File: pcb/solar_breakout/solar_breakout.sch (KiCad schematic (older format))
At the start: 29 parts

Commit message: Initial symbol fields
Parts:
- C?: footprint (none) -> agg:0402; Farnell (none) -> 2688503
- C?: footprint (none) -> agg:0402; Farnell (none) -> 2332546
- C?: footprint (none) -> agg:0603; Farnell (none) -> 2189109
- C?: footprint (none) -> agg:0402; Farnell Value -> 2533782
- C?: footprint (none) -> agg:0402; Farnell Value -> 2525061
- L?: footprint (none) -> agg:0402; Farnell Value -> 2042936
- R?: footprint (none) -> agg:0402; Farnell (none) -> 1458807
- R?: footprint (none) -> agg:0603; Farnell (none) -> 2447431
- R?: footprint (none) -> agg:0402
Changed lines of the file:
@@
 EESchema Schematic File Version 4
-LIBS:solar_breakout-cache
-EELAYER 26 0
+EELAYER 29 0
 EELAYER END
 $Descr A4 11693 8268
@@
 F 0 "R?" V 6700 3400 50  0000 L CNN
 F 1 "510k" V 6800 3350 50  0000 L CNN
-F 2 "" H 6700 3550 50  0001 C CNN
-F 3 "" H 6700 3550 50  0001 C CNN
+F 2 "agg:0402" H 6700 3550 50  0001 C CNN
+F 3 "https://uk.farnell.com/yageo/rc0402fr-07510kl/res-510k-1-0-063w-0402-thick-film/dp/1458807" H 6700 3550 50  0001 C CNN
+F 4 "1458807" H 0   0   50  0001 C CNN "Farnell"
 	1    6700 3550
 	0    1    1    0
@@
 F 0 "R?" V 6700 3250 50  0000 C CNN
 F 1 "750k" V 6800 3250 50  0000 C CNN
-F 2 "" H 6700 3350 50  0001 C CNN
-F 3 "" H 6700 3350 50  0001 C CNN
+F 2 "agg:0603" H 6700 3350 50  0001 C CNN
+F 3 "http://www.farnell.com/datasheets/2563624.pdf" H 6700 3350 50  0001 C CNN
+F 4 "2447431" H 0   0   50  0001 C CNN "Farnell"
 	1    6700 3350
 	0    1    1    0
@@
 F 0 "L?" H 5800 3078 50  0000 C CNN
 F 1 "10u" H 5800 2987 50  0000 C CNN
-F 2 "" H 5750 2900 50  0001 C CNN
-F 3 "" H 5750 2900 50  0001 C CNN
-F 4 "Value" H 5750 2900 60  0001 C CNN "Farnell"
+F 2 "agg:0402" H 5750 2900 50  0001 C CNN
+F 3 "http://www.farnell.com/datasheets/2050066.pdf" H 5750 2900 50  0001 C CNN
+F 4 "2042936" H 5750 2900 60  0001 C CNN "Farnell"
 	1    5750 2900
 	1    0    0    -1
@@
 F 0 "C?" V 6354 3908 50  0000 L CNN
 F 1 "4.7u" V 6445 3908 50  0000 L CNN
-F 2 "" H 6350 3850 50  0001 C CNN
-F 3 "" H 6350 3850 50  0001 C CNN
+F 2 "agg:0402" H 6350 3850 50  0001 C CNN
+F 3 "http://www.farnell.com/datasheets/2189109.pdf" H 6350 3850 50  0001 C CNN
+F 4 "2688503" H 0   0   50  0001 C CNN "Farnell"
 	1    6350 3850
 	0    1    1    0
@@
 F 0 "C?" V 5054 3658 50  0000 L CNN
 F 1 "10n" V 5145 3658 50  0000 L CNN
-F 2 "" H 5050 3600 50  0001 C CNN
-F 3 "" H 5050 3600 50  0001 C CNN
+F 2 "agg:0402" H 5050 3600 50  0001 C CNN
+F 3 "http://www.farnell.com/datasheets/2237835.pdf" H 5050 3600 50  0001 C CNN
+F 4 "2332546" H 0   0   50  0001 C CNN "Farnell"
 	1    5050 3600
 	0    1    1    0
@@
 F 0 "C?" H 5300 3005 50  0000 C CNN
 F 1 "10u" H 5300 3096 50  0000 C CNN
-F 2 "" H 5250 3200 50  0001 C CNN
-F 3 "" H 5250 3200 50  0001 C CNN
+F 2 "agg:0603" H 5250 3200 50  0001 C CNN
+F 3 "http://www.farnell.com/datasheets/2291921.pdf" H 5250 3200 50  0001 C CNN
+F 4 "2189109" H 0   0   50  0001 C CNN "Farnell"
 	1    5250 3200
 	-1   0    0    1
@@
 	5050 3200 5150 3200
 Wire Wire Line
-	3600 2900 5750 2900
+	3600 2900 5300 2900
 Wire Wire Line
 	5300 2900 5300 3200
 Wire Wire Line
-	5250 3200 5400 3200
+	5250 3200 5300 3200
 Connection ~ 5300 2900
 Connection ~ 5300 3200
 Wire Wire Line
-	6200 3500 6700 3500
-Wire Wire Line
-	6200 3300 7600 3300
+	6200 3500 6250 3500
+Wire Wire Line
+	6200 3300 6250 3300
 Connection ~ 6350 4050
 Text Label 4950 2900 0    50   ~ 0
@@
 F 0 "C?" V 6346 3392 50  0000 R CNN
 F 1 "22p" V 6255 3392 50  0000 R CNN
-F 2 "" H 6250 3450 50  0001 C CNN
-F 3 "" H 6250 3450 50  0001 C CNN
-F 4 "Value" H 6250 3450 60  0001 C CNN "Farnell"
+F 2 "agg:0402" H 6250 3450 50  0001 C CNN
+F 3 "http://www.farnell.com/datasheets/2031615.pdf" H 6250 3450 50  0001 C CNN
+F 4 "2533782" H 6250 3450 60  0001 C CNN "Farnell"
 	1    6250 3450
 	0    -1   -1   0
@@
 F 0 "C?" V 6904 3508 50  0000 L CNN
 F 1 "1u" V 6995 3508 50  0000 L CNN
-F 2 "" H 6900 3450 50  0001 C CNN
-F 3 "" H 6900 3450 50  0001 C CNN
-F 4 "Value" H 6900 3450 60  0001 C CNN "Farnell"
+F 2 "agg:0402" H 6900 3450 50  0001 C CNN
+F 3 "http://www.farnell.com/datasheets/2291921.pdf" H 6900 3450 50  0001 C CNN
+F 4 "2525061" H 6900 3450 60  0001 C CNN "Farnell"
 	1    6900 3450
 	0    1    1    0
@@
 Connection ~ 6900 3300
 Wire Wire Line
-	6700 3450 6700 3550
+	6700 3450 6700 3500
 Wire Wire Line
 	6700 3350 6700 3300
@@
 $EndComp
 Wire Wire Line
-	2950 3300 3100 3300
+	2950 3300 3000 3300
 Wire Wire Line
 	3100 3300 3100 3350
 Wire Wire Line
-	2950 3200 3300 3200
-Wire Wire Line
-	2950 1700 3300 1700
-Wire Wire Line
-	2950 1800 3100 1800
+	2950 3200 3000 3200
+Wire Wire Line
+	2950 1700 3000 1700
+Wire Wire Line
+	2950 1800 3000 1800
 Wire Wire Line
 	3100 1800 3100 1850
@@
 	7400 3800 7400 4050
 Wire Wire Line
-	4800 4050 7400 4050
+	4800 4050 5050 4050
 $Comp
 L agg-kicad:PART X?
@@
 $EndComp
 Wire Wire Line
-	4650 3650 4800 3650
-Wire Wire Line
-	4650 3750 4800 3750
+	4650 3650 4700 3650
+Wire Wire Line
+	4650 3750 4700 3750
 Text Label 750  7500 0    60   ~ 0
 Array_1_-
@@
 F 0 "R?" H 5350 3222 50  0000 C CNN
 F 1 "R" H 5350 3313 50  0000 C CNN
-F 2 "" H 5300 3400 50  0001 C CNN
+F 2 "agg:0402" H 5300 3400 50  0001 C CNN
 F 3 "" H 5300 3400 50  0001 C CNN
 F 4 "Value" H 5300 3400 60  0001 C CNN "Farnell"
@@
 	5300 3400 5400 3400
 Wire Wire Line
-	4800 3400 5200 3400
+	4800 3400 5050 3400
 Connection ~ 5050 3400
 Text Notes 5900 2850 0    60   ~ 0
@@
 	-1   0    0    1
 $EndComp
+Wire Wire Line
+	5800 4050 6250 4050
+Wire Wire Line
+	6250 4050 6350 4050
+Wire Wire Line
+	5300 4050 5350 4050
+Wire Wire Line
+	5050 4050 5300 4050
+Wire Wire Line
+	5350 4050 5800 4050
+Wire Wire Line
+	5300 2900 5750 2900
+Wire Wire Line
+	5300 3200 5400 3200
+Wire Wire Line
+	6350 4050 6700 4050
+Wire Wire Line
+	6250 3300 6700 3300
+Wire Wire Line
+	6250 3500 6700 3500
+Wire Wire Line
+	7150 3300 7400 3300
+Wire Wire Line
+	6900 3300 7150 3300
+Wire Wire Line
+	6700 3300 6900 3300
+Wire Wire Line
+	6700 3500 6700 3550
+Wire Wire Line
+	6700 4050 6900 4050
+Wire Wire Line
+	6900 4050 7150 4050
+Wire Wire Line
+	7400 3300 7600 3300
+Wire Wire Line
+	7150 4050 7400 4050
+Wire Wire Line
+	3000 3300 3100 3300
+Wire Wire Line
+	3000 3200 3300 3200
+Wire Wire Line
+	3000 1800 3100 1800
+Wire Wire Line
+	3000 1700 3300 1700
+Wire Wire Line
+	4700 3650 4800 3650
+Wire Wire Line
+	4700 3750 4800 3750
+Wire Wire Line
+	5050 3400 5200 3400
 $EndSCHEMATC

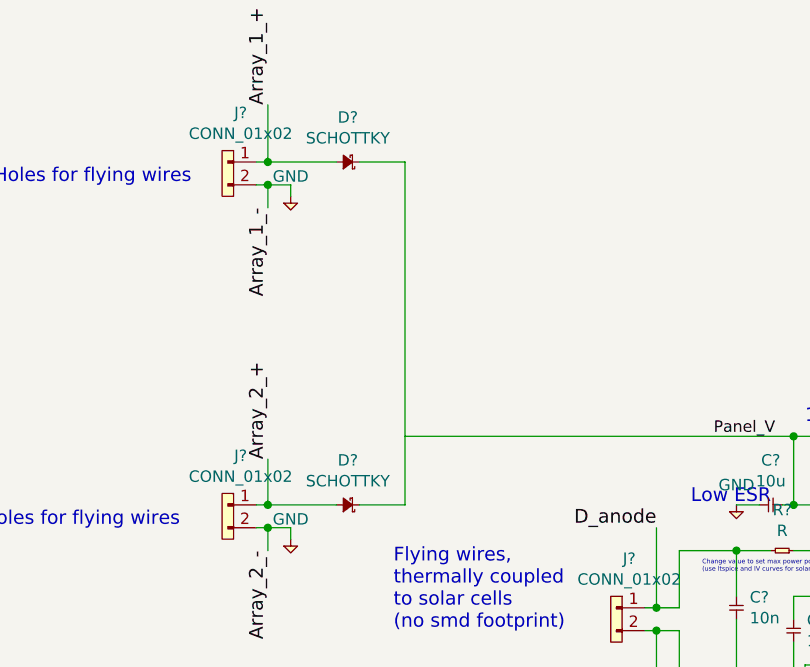
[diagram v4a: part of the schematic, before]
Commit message: Tidy some schematic errors
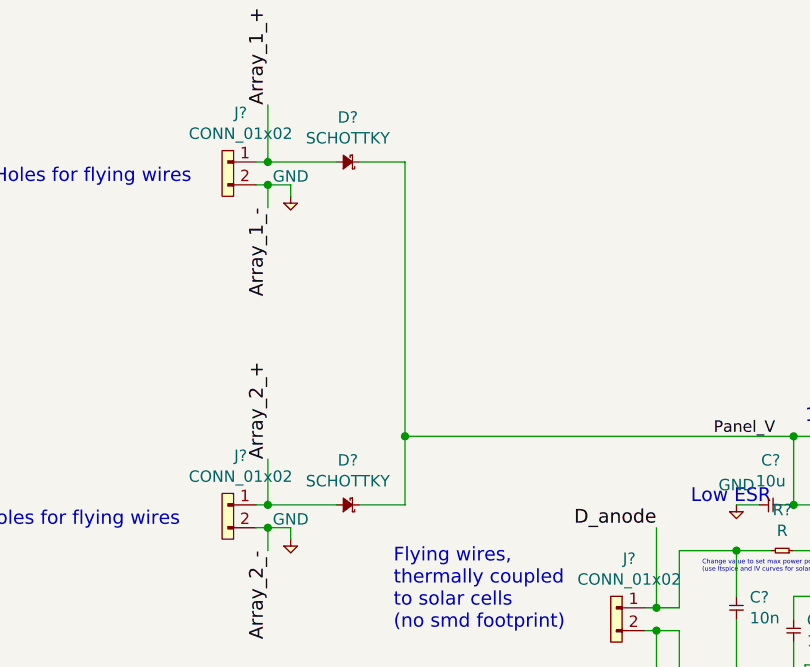
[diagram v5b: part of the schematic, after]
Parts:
- C?: Farnell 2189109 -> (none)
- C?: footprint agg:0402 -> (none); Farnell 2525061 -> (none)
- L?: footprint agg:0402 -> (none); Farnell 2042936 -> (none)
- R?: footprint agg:0402 -> (none)
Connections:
- net Panel_V: now also D?.1, D?.1
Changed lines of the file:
@@
 F 0 "L?" H 5800 3078 50  0000 C CNN
 F 1 "10u" H 5800 2987 50  0000 C CNN
-F 2 "agg:0402" H 5750 2900 50  0001 C CNN
-F 3 "http://www.farnell.com/datasheets/2050066.pdf" H 5750 2900 50  0001 C CNN
-F 4 "2042936" H 5750 2900 60  0001 C CNN "Farnell"
+F 2 "" H 5750 2900 50  0001 C CNN
+F 3 "" H 5750 2900 50  0001 C CNN
 	1    5750 2900
 	1    0    0    -1
@@
 F 2 "agg:0603" H 5250 3200 50  0001 C CNN
 F 3 "http://www.farnell.com/datasheets/2291921.pdf" H 5250 3200 50  0001 C CNN
-F 4 "2189109" H 0   0   50  0001 C CNN "Farnell"
 	1    5250 3200
 	-1   0    0    1
@@
 F 0 "C?" V 6904 3508 50  0000 L CNN
 F 1 "1u" V 6995 3508 50  0000 L CNN
-F 2 "agg:0402" H 6900 3450 50  0001 C CNN
-F 3 "http://www.farnell.com/datasheets/2291921.pdf" H 6900 3450 50  0001 C CNN
-F 4 "2525061" H 6900 3450 60  0001 C CNN "Farnell"
+F 2 "" H 6900 3450 50  0001 C CNN
+F 3 "" H 6900 3450 50  0001 C CNN
 	1    6900 3450
 	0    1    1    0
@@
 	3400 3200 3600 3200
 Wire Wire Line
-	3600 1700 3600 3200
-Wire Wire Line
 	3400 1700 3600 1700
 $Comp
@@
 F 0 "R?" H 5350 3222 50  0000 C CNN
 F 1 "R" H 5350 3313 50  0000 C CNN
-F 2 "agg:0402" H 5300 3400 50  0001 C CNN
+F 2 "" H 5300 3400 50  0001 C CNN
 F 3 "" H 5300 3400 50  0001 C CNN
 F 4 "Value" H 5300 3400 60  0001 C CNN "Farnell"
@@
 Wire Wire Line
 	5050 3400 5200 3400
+Wire Wire Line
+	3600 1700 3600 2900
+Wire Wire Line
+	3600 2900 3600 3200
+Connection ~ 3600 2900
 $EndSCHEMATC

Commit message: Fix some symbol fields
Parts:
- C?: Farnell 2332546 -> 1327624
- C?: footprint agg:0603 -> agg:1206; Farnell (none) -> 1135175
- C?: Farnell 2495145 -> (none)
- R?: footprint (none) -> agg:0603
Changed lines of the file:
@@
 EESchema Schematic File Version 4
+LIBS:solar_breakout-cache
 EELAYER 29 0
 EELAYER END
@@
 F 2 "agg:0402" H 5050 3600 50  0001 C CNN
 F 3 "http://www.farnell.com/datasheets/2237835.pdf" H 5050 3600 50  0001 C CNN
-F 4 "2332546" H 0   0   50  0001 C CNN "Farnell"
+F 4 "1327624" H 0   0   50  0001 C CNN "Farnell"
 	1    5050 3600
 	0    1    1    0
@@
 F 0 "C?" H 5300 3005 50  0000 C CNN
 F 1 "10u" H 5300 3096 50  0000 C CNN
-F 2 "agg:0603" H 5250 3200 50  0001 C CNN
-F 3 "http://www.farnell.com/datasheets/2291921.pdf" H 5250 3200 50  0001 C CNN
+F 2 "agg:1206" H 5250 3200 50  0001 C CNN
+F 3 "http://www.farnell.com/datasheets/2096548.pdf" H 5250 3200 50  0001 C CNN
+F 4 "1135175" H 0   0   50  0001 C CNN "Farnell"
 	1    5250 3200
 	-1   0    0    1
@@
 F 2 "agg:0402" H 5300 3700 50  0001 C CNN
 F 3 "" H 5300 3700 50  0001 C CNN
-F 4 "2495145" H 5300 3700 60  0001 C CNN "Farnell"
 	1    5300 3700
 	0    1    1    0
@@
 F 0 "R?" H 5350 3222 50  0000 C CNN
 F 1 "R" H 5350 3313 50  0000 C CNN
-F 2 "" H 5300 3400 50  0001 C CNN
+F 2 "agg:0603" H 5300 3400 50  0001 C CNN
 F 3 "" H 5300 3400 50  0001 C CNN
 F 4 "Value" H 5300 3400 60  0001 C CNN "Farnell"

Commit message: Fill in more symbol fields
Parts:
- C?: footprint agg:0402 -> agg:0603; Farnell (none) -> 2470448
- C?: footprint (none) -> agg:0603; Farnell (none) -> 2470448
- L?: footprint (none) -> agg:0805; Farnell (none) -> 2286356
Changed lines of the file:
@@
 F 0 "L?" H 5800 3078 50  0000 C CNN
 F 1 "10u" H 5800 2987 50  0000 C CNN
-F 2 "" H 5750 2900 50  0001 C CNN
-F 3 "" H 5750 2900 50  0001 C CNN
+F 2 "agg:0805" H 5750 2900 50  0001 C CNN
+F 3 "http://www.farnell.com/datasheets/1681885.pdf" H 5750 2900 50  0001 C CNN
+F 4 "2286356" H 0   0   50  0001 C CNN "Farnell"
 	1    5750 2900
 	1    0    0    -1
@@
 F 0 "C?" V 5304 3758 50  0000 L CNN
 F 1 "1u" V 5395 3758 50  0000 L CNN
-F 2 "agg:0402" H 5300 3700 50  0001 C CNN
-F 3 "" H 5300 3700 50  0001 C CNN
+F 2 "agg:0603" H 5300 3700 50  0001 C CNN
+F 3 "http://www.farnell.com/datasheets/2048284.pdf" H 5300 3700 50  0001 C CNN
+F 4 "2470448" H 0   0   50  0001 C CNN "Farnell"
 	1    5300 3700
 	0    1    1    0
@@
 F 0 "C?" V 6904 3508 50  0000 L CNN
 F 1 "1u" V 6995 3508 50  0000 L CNN
-F 2 "" H 6900 3450 50  0001 C CNN
-F 3 "" H 6900 3450 50  0001 C CNN
+F 2 "agg:0603" H 6900 3450 50  0001 C CNN
+F 3 "http://www.farnell.com/datasheets/2048284.pdf" H 6900 3450 50  0001 C CNN
+F 4 "2470448" H 0   0   50  0001 C CNN "Farnell"
 	1    6900 3450
 	0    1    1    0

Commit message: Add values for super capacitor
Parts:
- C?: Farnell (none) -> 2696619
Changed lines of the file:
@@
 F 1 "50" V 7155 3492 50  0000 R CNN
 F 2 "" H 7150 3550 50  0001 C CNN
-F 3 "" H 7150 3550 50  0001 C CNN
+F 3 "http://www.farnell.com/datasheets/2675068.pdf" H 7150 3550 50  0001 C CNN
+F 4 "2696619" H 0   0   50  0001 C CNN "Farnell"
 	1    7150 3550
 	0    -1   -1   0
